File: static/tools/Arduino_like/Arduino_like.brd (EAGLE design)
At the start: 63.5 x 41.6 mm, 19 parts, among them IC1 MEGA8-P

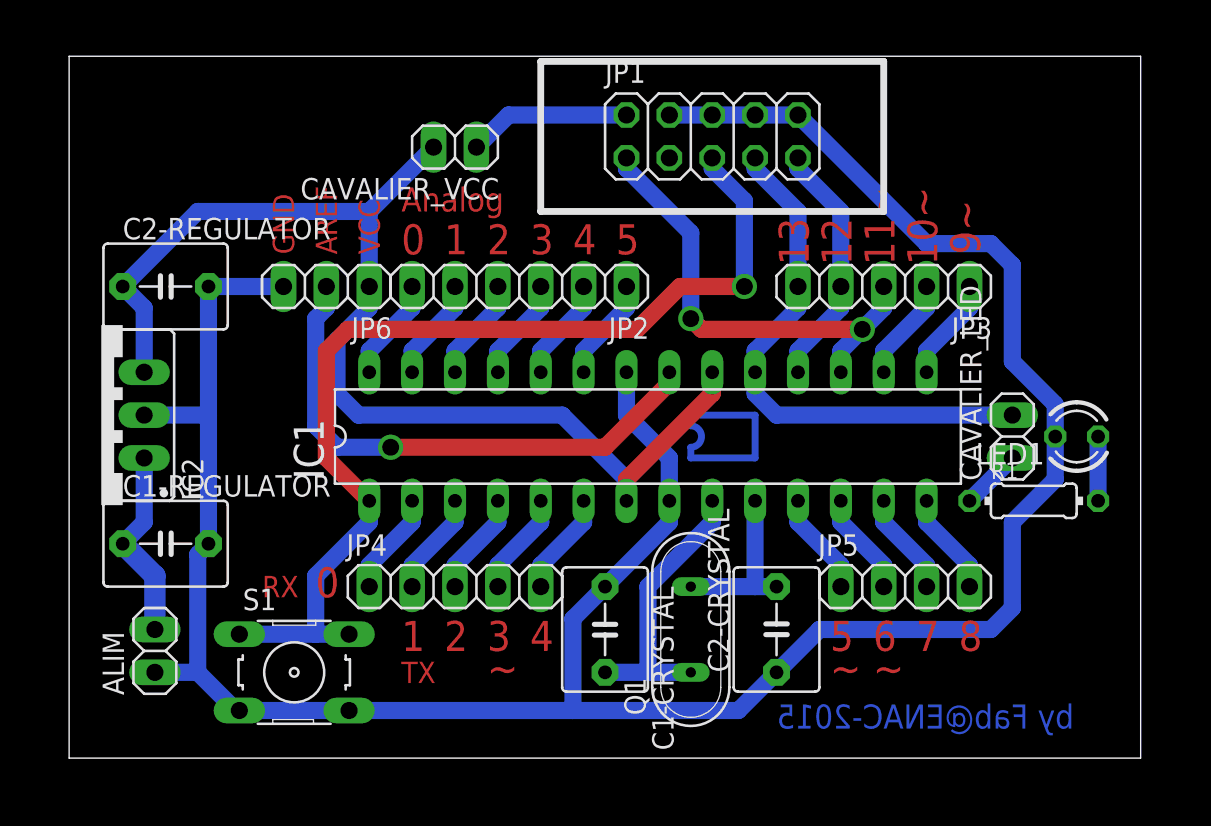
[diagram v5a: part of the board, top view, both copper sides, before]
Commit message: [arduino like] move via.
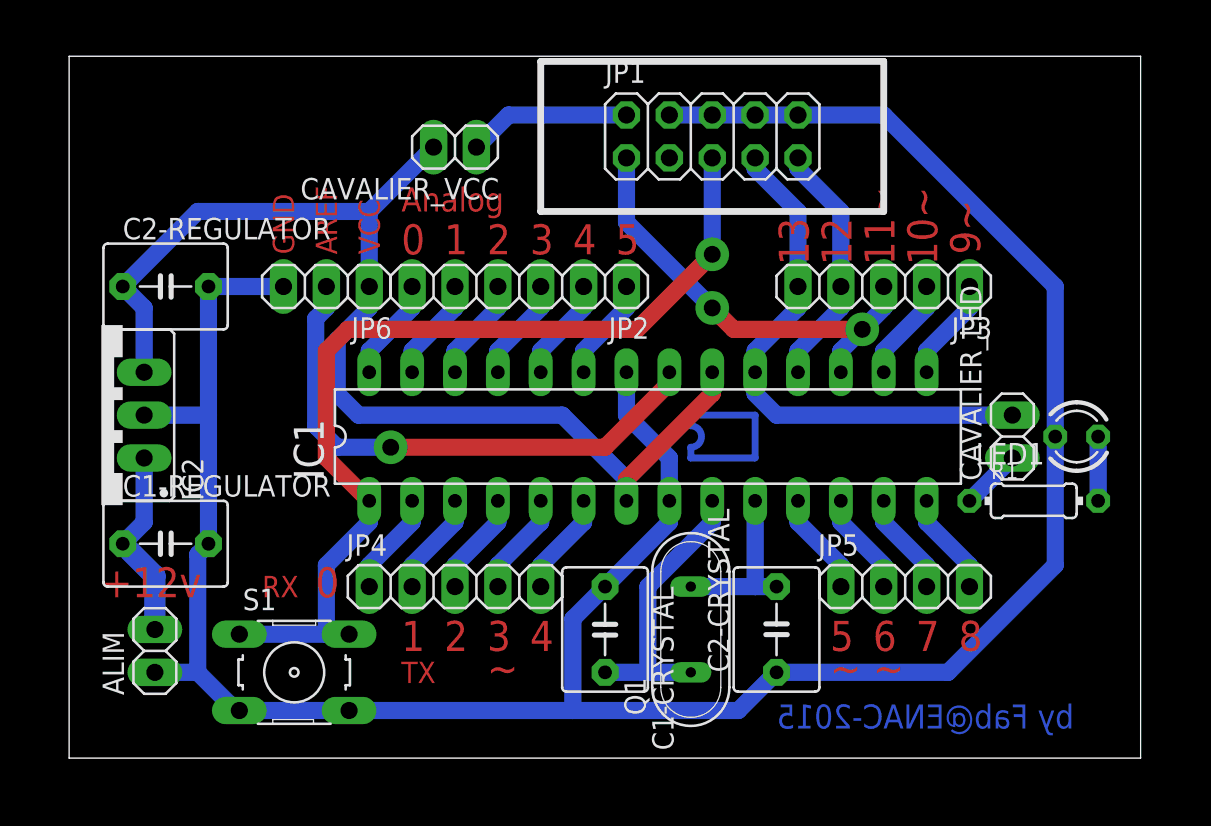
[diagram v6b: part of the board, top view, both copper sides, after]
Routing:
- net N$4: track 60.4 -> 56.3 mm
- net N$3: track 27.7 -> 26.5 mm
- net GND: track 155.8 -> 156.5 mm
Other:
- board text added: "+12v"

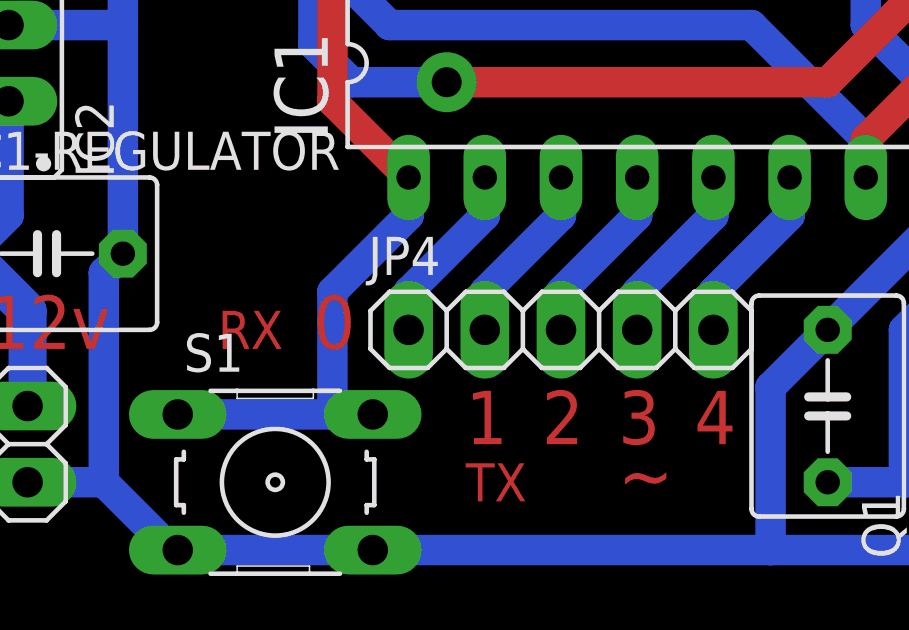
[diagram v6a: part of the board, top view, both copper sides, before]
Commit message: [Arduino_like] add reset pin.
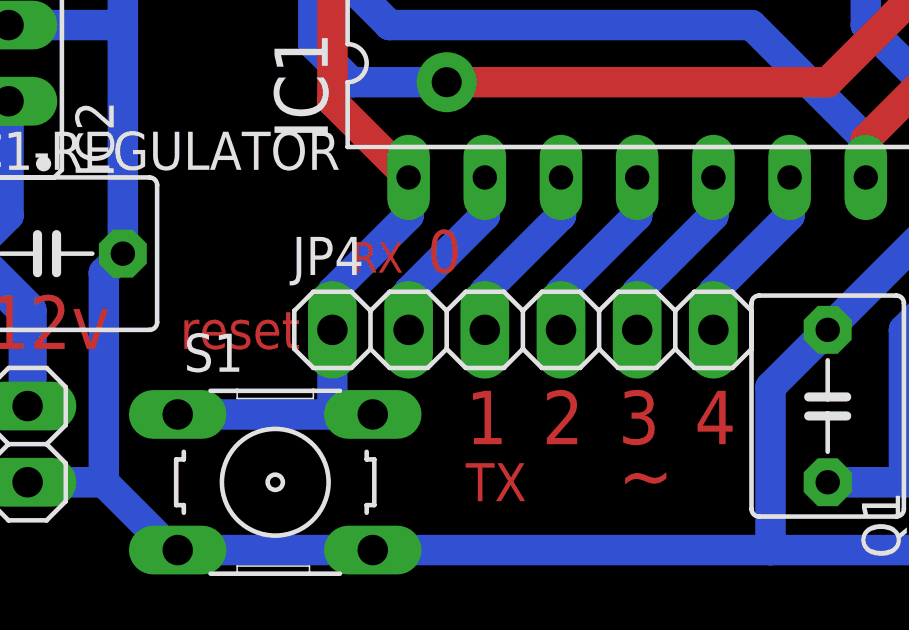
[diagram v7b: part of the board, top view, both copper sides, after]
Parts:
- JP4: device pinhead:1X05 -> pinhead:1X06
- moved JP4 1.27 mm to (21.6, 10.2)
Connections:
- net N$14: now also JP4.2; no longer JP4.1
- net N$16: now also JP4.3; no longer JP4.2
- net N$17: now also JP4.4; no longer JP4.3
- net N$18: now also JP4.5; no longer JP4.4
- net N$19: now also JP4.6; no longer JP4.5
- net N$4: now also JP4.1
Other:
- board text added: "reset"
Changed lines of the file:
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@@
 <layer number="21" name="tPlace" color="7" fill="1" visible="yes" active="yes"/>
 <layer number="22" name="bPlace" color="7" fill="1" visible="yes" active="yes"/>
-<layer number="23" name="tOrigins" color="15" fill="1" visible="yes" active="yes"/>
-<layer number="24" name="bOrigins" color="15" fill="1" visible="yes" active="yes"/>
-<layer number="25" name="tNames" color="7" fill="1" visible="yes" active="yes"/>
-<layer number="26" name="bNames" color="7" fill="1" visible="yes" active="yes"/>
-<layer number="27" name="tValues" color="7" fill="1" visible="yes" active="yes"/>
-<layer number="28" name="bValues" color="7" fill="1" visible="yes" active="yes"/>
-<layer number="29" name="tStop" color="7" fill="3" visible="yes" active="yes"/>
-<layer number="30" name="bStop" color="7" fill="6" visible="yes" active="yes"/>
-<layer number="31" name="tCream" color="7" fill="4" visible="yes" active="yes"/>
-<layer number="32" name="bCream" color="7" fill="5" visible="yes" active="yes"/>
-<layer number="33" name="tFinish" color="6" fill="3" visible="yes" active="yes"/>
-<layer number="34" name="bFinish" color="6" fill="6" visible="yes" active="yes"/>
-<layer number="35" name="tGlue" color="7" fill="4" visible="yes" active="yes"/>
-<layer number="36" name="bGlue" color="7" fill="5" visible="yes" active="yes"/>
-<layer number="37" name="tTest" color="7" fill="1" visible="yes" active="yes"/>
-<layer number="38" name="bTest" color="7" fill="1" visible="yes" active="yes"/>
-<layer number="39" name="tKeepout" color="4" fill="11" visible="yes" active="yes"/>
-<layer number="40" name="bKeepout" color="1" fill="11" visible="yes" active="yes"/>
-<layer number="41" name="tRestrict" color="4" fill="10" visible="yes" active="yes"/>
-<layer number="42" name="bRestrict" color="1" fill="10" visible="yes" active="yes"/>
-<layer number="43" name="vRestrict" color="2" fill="10" visible="yes" active="yes"/>
-<layer number="44" name="Drills" color="7" fill="1" visible="yes" active="yes"/>
-<layer number="45" name="Holes" color="7" fill="1" visible="yes" active="yes"/>
-<layer number="46" name="Milling" color="3" fill="1" visible="yes" active="yes"/>
-<layer number="47" name="Measures" color="7" fill="1" visible="yes" active="yes"/>
-<layer number="48" name="Document" color="7" fill="1" visible="yes" active="yes"/>
-<layer number="49" name="Reference" color="7" fill="1" visible="yes" active="yes"/>
-<layer number="51" name="tDocu" color="7" fill="1" visible="yes" active="yes"/>
-<layer number="52" name="bDocu" color="7" fill="1" visible="yes" active="yes"/>
+<layer number="23" name="tOrigins" color="15" fill="1" visible="no" active="yes"/>
+<layer number="24" name="bOrigins" color="15" fill="1" visible="no" active="yes"/>
+<layer number="25" name="tNames" color="7" fill="1" visible="no" active="yes"/>
+<layer number="26" name="bNames" color="7" fill="1" visible="no" active="yes"/>
+<layer number="27" name="tValues" color="7" fill="1" visible="no" active="yes"/>
+<layer number="28" name="bValues" color="7" fill="1" visible="no" active="yes"/>
+<layer number="29" name="tStop" color="7" fill="3" visible="no" active="yes"/>
+<layer number="30" name="bStop" color="7" fill="6" visible="no" active="yes"/>
+<layer number="31" name="tCream" color="7" fill="4" visible="no" active="yes"/>
+<layer number="32" name="bCream" color="7" fill="5" visible="no" active="yes"/>
+<layer number="33" name="tFinish" color="6" fill="3" visible="no" active="yes"/>
+<layer number="34" name="bFinish" color="6" fill="6" visible="no" active="yes"/>
+<layer number="35" name="tGlue" color="7" fill="4" visible="no" active="yes"/>
+<layer number="36" name="bGlue" color="7" fill="5" visible="no" active="yes"/>
+<layer number="37" name="tTest" color="7" fill="1" visible="no" active="yes"/>
+<layer number="38" name="bTest" color="7" fill="1" visible="no" active="yes"/>
+<layer number="39" name="tKeepout" color="4" fill="11" visible="no" active="yes"/>
+<layer number="40" name="bKeepout" color="1" fill="11" visible="no" active="yes"/>
+<layer number="41" name="tRestrict" color="4" fill="10" visible="no" active="yes"/>
+<layer number="42" name="bRestrict" color="1" fill="10" visible="no" active="yes"/>
+<layer number="43" name="vRestrict" color="2" fill="10" visible="no" active="yes"/>
+<layer number="44" name="Drills" color="7" fill="1" visible="no" active="yes"/>
+<layer number="45" name="Holes" color="7" fill="1" visible="no" active="yes"/>
+<layer number="46" name="Milling" color="3" fill="1" visible="no" active="yes"/>
+<layer number="47" name="Measures" color="7" fill="1" visible="no" active="yes"/>
+<layer number="48" name="Document" color="7" fill="1" visible="no" active="yes"/>
+<layer number="49" name="Reference" color="7" fill="1" visible="no" active="yes"/>
+<layer number="51" name="tDocu" color="7" fill="1" visible="no" active="yes"/>
+<layer number="52" name="bDocu" color="7" fill="1" visible="no" active="yes"/>
 <layer number="91" name="Nets" color="2" fill="1" visible="no" active="no"/>
 <layer number="92" name="Busses" color="1" fill="1" visible="no" active="no"/>
@@
 <wire x1="63.48" y1="41.58" x2="0" y2="41.58" width="0" layer="20"/>
 <wire x1="0" y1="41.58" x2="0" y2="0" width="0" layer="20"/>
-<text x="14.605" y="9.525" size="1.778" layer="1">0</text>
+<text x="18.415" y="12.065" size="1.4224" layer="1">0</text>
 <text x="19.685" y="6.35" size="1.778" layer="1">1</text>
 <text x="22.225" y="6.35" size="1.778" layer="1">2</text>
@@
 <text x="47.625" y="4.445" size="1.778" layer="1">~</text>
 <text x="19.685" y="4.445" size="1.27" layer="1">TX</text>
-<text x="11.43" y="9.525" size="1.27" layer="1">RX</text>
+<text x="15.875" y="12.065" size="1.016" layer="1">RX</text>
 <wire x1="27.94" y1="41.275" x2="27.94" y2="32.385" width="0.4064" layer="21"/>
 <wire x1="27.94" y1="41.275" x2="48.26" y2="41.275" width="0.4064" layer="21"/>
@@
 <dimension x1="43.18" y1="27.94" x2="33.02" y2="27.94" x3="38.1" y3="48.26" layer="47"/>
 <text x="1.905" y="9.525" size="1.778" layer="1">+12v</text>
+<text x="10.16" y="9.525" size="1.27" layer="1">reset</text>
 </plain>
 <attributes>
@@
 <attribute name="OC_FARNELL" value="176432" x="13.335" y="5.08" size="1.778" layer="27" display="off"/>
 </element>
-<element name="JP4" library="pinhead" package="1X05" value="" x="22.86" y="10.16"/>
 <element name="JP3" library="pinhead" package="1X05" value="" x="48.26" y="27.94" rot="R180"/>
 <element name="JP5" library="pinhead" package="1X04" value="" x="49.53" y="10.16"/>
 <element name="JP6" library="pinhead" package="1X03" value="" x="15.24" y="27.94" rot="R180"/>
+<element name="JP4" library="pinhead" package="1X06" value="" x="21.59" y="10.16"/>
 </elements>
 <signals>
@@
 <wire x1="15.24" y1="7.3406" x2="16.5862" y2="7.3406" width="1.016" layer="16"/>
 <wire x1="17.78" y1="15.24" x2="17.78" y2="13.97" width="1.016" layer="16"/>
-<wire x1="17.78" y1="13.97" x2="15.24" y2="11.43" width="1.016" layer="16"/>
-<wire x1="15.24" y1="11.43" x2="15.24" y2="7.3406" width="1.016" layer="16"/>
+<contactref element="JP4" pad="1"/>
+<wire x1="15.24" y1="10.16" x2="15.24" y2="7.3406" width="1.016" layer="16"/>
+<wire x1="15.24" y1="10.16" x2="15.24" y2="11.43" width="1.016" layer="16"/>
+<wire x1="15.24" y1="11.43" x2="17.78" y2="13.97" width="1.016" layer="16"/>
 </signal>
 <signal name="VCC">
@@
 <signal name="N$14">
 <contactref element="IC1" pad="2"/>
-<contactref element="JP4" pad="1"/>
-<wire x1="17.78" y1="10.16" x2="17.78" y2="11.43" width="1.016" layer="16"/>
 <wire x1="17.78" y1="11.43" x2="20.32" y2="13.97" width="1.016" layer="16"/>
 <wire x1="20.32" y1="13.97" x2="20.32" y2="15.24" width="1.016" layer="16"/>
+<contactref element="JP4" pad="2"/>
+<wire x1="17.78" y1="11.43" x2="17.78" y2="10.16" width="1.016" layer="16"/>
 </signal>
 <signal name="N$16">
 <contactref element="IC1" pad="3"/>
-<contactref element="JP4" pad="2"/>
-<wire x1="20.32" y1="10.16" x2="20.32" y2="11.43" width="1.016" layer="16"/>
 <wire x1="20.32" y1="11.43" x2="22.86" y2="13.97" width="1.016" layer="16"/>
 <wire x1="22.86" y1="13.97" x2="22.86" y2="15.24" width="1.016" layer="16"/>
+<contactref element="JP4" pad="3"/>
+<wire x1="20.32" y1="11.43" x2="20.32" y2="10.16" width="1.016" layer="16"/>
 </signal>
 <signal name="N$17">
 <contactref element="IC1" pad="4"/>
-<contactref element="JP4" pad="3"/>
-<wire x1="22.86" y1="10.16" x2="22.86" y2="11.43" width="1.016" layer="16"/>
 <wire x1="22.86" y1="11.43" x2="25.4" y2="13.97" width="1.016" layer="16"/>
 <wire x1="25.4" y1="13.97" x2="25.4" y2="15.24" width="1.016" layer="16"/>
+<contactref element="JP4" pad="4"/>
+<wire x1="22.86" y1="11.43" x2="22.86" y2="10.16" width="1.016" layer="16"/>
 </signal>
 <signal name="N$18">
 <contactref element="IC1" pad="5"/>
-<contactref element="JP4" pad="4"/>
-<wire x1="25.4" y1="10.16" x2="25.4" y2="11.43" width="1.016" layer="16"/>
 <wire x1="25.4" y1="11.43" x2="27.94" y2="13.97" width="1.016" layer="16"/>
 <wire x1="27.94" y1="13.97" x2="27.94" y2="15.24" width="1.016" layer="16"/>
+<contactref element="JP4" pad="5"/>
+<wire x1="25.4" y1="11.43" x2="25.4" y2="10.16" width="1.016" layer="16"/>
 </signal>
 <signal name="N$19">
 <contactref element="IC1" pad="6"/>
-<contactref element="JP4" pad="5"/>
-<wire x1="27.94" y1="10.16" x2="27.94" y2="11.43" width="1.016" layer="16"/>
 <wire x1="27.94" y1="11.43" x2="30.48" y2="13.97" width="1.016" layer="16"/>
 <wire x1="30.48" y1="13.97" x2="30.48" y2="15.24" width="1.016" layer="16"/>
+<contactref element="JP4" pad="6"/>
+<wire x1="27.94" y1="11.43" x2="27.94" y2="10.16" width="1.016" layer="16"/>
 </signal>
 <signal name="N$20">
@@
 </signal>
 </signals>
+<errors>
+</errors>
 </board>
 </drawing>

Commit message: [Arduino_like] move text.
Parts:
- moved ALIM 1.80 mm to (6.35, 7.62), turned to 180 degrees
- moved S1 1.42 mm to (14.6, 4.45)
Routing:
- net GND: track 156.5 -> 154.1 mm
- net N$4: track 56.3 -> 57.0 mm
